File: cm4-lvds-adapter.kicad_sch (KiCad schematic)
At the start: 19 parts, among them J1 Plug_Molex_SlimStack_2x15_538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, J2 JST_SM_1x10_SM10B-SURS-TF-LF-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

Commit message: [#54932] Add changes requested in review
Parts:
- removed C1: C_100n_0402, antmicro-footprints:C_0402_1005Metric, symbol antmicroCapacitors0402:C_100n_0402
- removed TP2, TP4: TP_1mm_SMD, antmicro-footprints:TP_SMD_1mm, symbol antmicroTestPoints:TP_1mm_SMD
- added C1, C6: C_10u_0402, antmicro-footprints:C_0402_1005Metric, symbol antmicroCapacitors0402:C_10u_0402
- added C10, C4, C42, C44, C45, C46, C47, C5, C8, C9: C_100n_0402, antmicro-footprints:C_0402_1005Metric, symbol antmicroCapacitors0402:C_100n_0402
- added C11, C12, C13: C_10n_0402, antmicro-footprints:C_0402_1005Metric, symbol antmicroCapacitors0402:C_10n_0402
- added C14, C7: C_1u_0402, antmicro-footprints:C_0402_1005Metric, symbol antmicroCapacitors0402:C_1u_0402
- added FB1: 220Z/2A, antmicro-footprints:FB_0603_1608Metric, symbol antmicroFerriteBeadsandChips:FB_220Z_2.2A_TDK-MPZ_0603
- added J3: Conn_FFC_Amphenol_62684-402100AHLF, antmicro-footprints:Conn_FFC_Amphenol_1x40_62684-402100AHLF, symbol antmicroFCCConnectors:FFC_Amphenol_1x40_62684-402100AHLF
- added R4, R5, R? (x2): R_4k7_0402, antmicro-footprints:R_0402_1005Metric, symbol antmicroResistors0402:R_4k7_0402
- added R40, R42, R45, R6, R7, R8: R_10k_0402, antmicro-footprints:R_0402_1005Metric, symbol antmicroResistors0402:R_10k_0402
- added R41, R43, R46: R_0R_0402, antmicro-footprints:R_0402_1005Metric, symbol antmicroResistors0402:R_0R_0402
- added R44: R_100k_0402, antmicro-footprints:R_0402_1005Metric, symbol antmicroResistors0402:R_100k_0402
- added TP? (x7): TP_0.75mm_SMD, antmicro-footprints:TP_SMD_0.75mm, symbol antmicroTestPoints:TP_0.75mm_SMD
- added U3: SN65DSI84, antmicro-footprints:HTQFP-64_10x10mm_P0.5mm, symbol antmicroInterfaceControllers:SN65DSI84
- added U?: NTS0104_DHVQFN, antmicro-footprints:DHVQFN-14-1EP_2.5x3mm, symbol antmicroLogicTranslatorsLevelShifters:NTS0104_DHVQFN
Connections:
- net AntmUD.~{RST} is gone; now on net DSICtrl.~{RST}: C43.2, R39.1, TP13.1
- net +3V3: now also C4.2, C47.2, J3.2, J3.3, R40.2, R42.2, R44.2, R45.2, R?.2, U?.14 (VCC_B)
- net +5V: now also C1.2
- net DSI.CLK_N: now also U3.25 (DACN)
- net DSI.CLK_P: now also U3.24 (DACP)
- net DSI.D0_N: now also U3.20 (DA0N)
- net DSI.D0_P: now also U3.19 (DA0P)
- net DSI.D1_N: now also U3.22 (DA1N)
- net DSI.D1_P: now also U3.21 (DA1P)
- net DSI.D2_N: now also U3.28 (DA2N)
- net DSI.D2_P: now also U3.27 (DA2P)
- net DSI.D3_N: now also U3.30 (DA3N)
- net DSI.D3_P: now also U3.29 (DA3P)
- net DSICtrl.EN: now also J3.6, R44.1, U?.11 (B3)
- net DSICtrl.IRQ1: now also R?.1, U?.10 (B4)
- net DSICtrl.SCL: now also U?.12 (B2)
- net DSICtrl.SDA: now also U?.13 (B1)
- net DSICtrl.~{RST}: now also J3.5
- net GND: now also C1.1, C10.1, C11.1, C12.1, C13.1, C14.1, C4.1, C42.1, C44.1, C45.1, C46.1, C47.1, C5.1, C6.1, C7.1, C8.1, C9.1, J3.10, J3.13, J3.16, J3.19, J3.22, J3.25, J3.30, J3.7, J3.SH, R41.2, R43.2, R46.2, R7.1, R8.2, U3.23 (GND), U3.26 (GND), U3.52 (GND), U3.65 (PAD), U?.15 (GNDPAD), U?.7 (GND)
- new net: C10.2, C11.2, C12.2, C13.2, C6.2, C7.2, C8.2, C9.2, FB1.2, U3.14 (VCC), U3.18 (VCC), U3.3 (VCC), U3.32 (VCC), U3.35 (VCC), U3.40 (VCC), U3.43 (VCC), U3.48 (VCC), U3.49 (VCC), U3.55 (VCC), U3.58 (VCC), U3.63 (VCC)
- new net: R6.1, R7.2, U3.64 (ADDR)
- new net: J3.26, TP?.1
- new net: J3.24, TP?.1
- new net: R8.1, U3.17 (REFCLK)
- new net: J3.37, TP?.1
- new net: J3.23, TP?.1
- new net: J3.27, TP?.1
- new net: J3.36, TP?.1
- new net: J3.4, TP?.1
- new net: C14.2, U3.31 (VCORE)
- new net +18V: C42.2, J3.38
- new net +1V8: C5.2, FB1.1, R4.2, R5.2, R6.2, R?.2, U?.1 (VCC_A), U?.8 (OE)
- new net +3V9: C45.2, J3.1
- new net +9V6: C44.2, J3.29
- new net +VLED: C46.2, J3.39, J3.40
- new net -6V: J3.35
- new net -VLED: J3.31, J3.32
- new net DSICtrl_1V8.EN: R?.1, U3.2 (EN), U?.4 (A3)
- new net DSICtrl_1V8.IRQ: U3.33 (IRQ), U?.5 (A4)
- new net DSICtrl_1V8.SCL: R5.1, U3.16 (SDA), U?.3 (A2)
- new net DSICtrl_1V8.SDA: R4.1, U3.15 (SCL), U?.2 (A1)
- new net LVDS.CLK_N: J3.17, U3.39 (A_CLKN)
- new net LVDS.CLK_P: J3.18, U3.38 (A_CLKP)
- new net LVDS.D0_N: J3.8, U3.47 (A_Y0N)
- new net LVDS.D0_P: J3.9, U3.46 (A_Y0P)
- new net LVDS.D1_N: J3.11, U3.45 (A_Y1N)
- new net LVDS.D1_P: J3.12, U3.44 (A_Y1P)
- new net LVDS.D2_N: J3.14, U3.42 (A_Y2N)
- new net LVDS.D2_P: J3.15, U3.41 (A_Y2P)
- new net LVDS.D3_N: J3.20, U3.37 (A_Y3N)
- new net LVDS.D3_P: J3.21, U3.36 (A_Y3P)
- new net SELB: J3.28, R40.1, R41.1
- new net SHLR: J3.33, R42.1, R43.1
- new net UPDN: J3.34, R45.1, R46.1
- no-connect marks 8 -> 18
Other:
- sheet LVDS display renamed Power
- removed sheet DSI -> LVDS converter
- sheet Power: file lvds.kicad_sch -> power.kicad_sch
- sheet Power ports: added none; removed LVDS{LVDS}
- note added: "Display configuration"
- note added: "Display decoupling capacitors"
- note added: "Max 45mA"
- note added: "Note: I_{2}C address selection: ADDR | write address 1 | 0x5A 0 | 0x58"
- note added: "Note: SN65DSI83*-Q1 should be here drop-in compatible"
- note added: "Set display orientation as NORMAL datasheet pg.10"
- note added: "VDD"
- note added: "Vcom"
- note added: "https://drive.google.com/file/d/1bkluVrM0Or-iIsGhq6TyBP5G7xjQ2-Zj/view"
- note added: "select 8bit input"
- moved on the sheet: C43, D1, D2, D3, D4, J1, J2, R1, R2, R39

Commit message: [#54932] Clean ERC
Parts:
- gave numbers to parts that had none: 10
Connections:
- net DSICtrl_1V8.IRQ: no longer U2.5 (A4)
- new net DSICtrl_1V8.IRQ1: U2.5 (A4)
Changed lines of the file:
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@@
     (effects (font (size 1.27 1.27)) (justify right bottom))
   )
-  (label "DSICtrl_1V8.IRQ" (at 161.29 190.5 0) (fields_autoplaced)
+  (label "DSICtrl_1V8.IRQ1" (at 161.29 190.5 0) (fields_autoplaced)
     (effects (font (size 1.27 1.27)) (justify left bottom))
   )
@@
   (symbol (lib_id "antmicroTestPoints:TP_0.75mm_SMD") (at 388.62 161.29 180) (unit 1)
     (in_bom yes) (on_board yes) (dnp no)
-    (property "Reference" "TP?" (at 382.27 161.29 0)
+    (property "Reference" "TP9" (at 382.27 161.29 0)
       (effects (font (size 1.27 1.27) (thickness 0.15)))
     )
@@
       (project "cm4-lvds-adapter"
         (path "/60b842dc-0853-4a25-99ac-5784ddf94d0d"
-          (reference "TP?") (unit 1)
+          (reference "TP9") (unit 1)
         )
       )
@@
   (symbol (lib_id "antmicroTestPoints:TP_0.75mm_SMD") (at 388.62 156.21 180) (unit 1)
     (in_bom yes) (on_board yes) (dnp no)
-    (property "Reference" "TP?" (at 382.27 156.21 0)
+    (property "Reference" "TP8" (at 382.27 156.21 0)
       (effects (font (size 1.27 1.27) (thickness 0.15)))
     )
@@
       (project "cm4-lvds-adapter"
         (path "/60b842dc-0853-4a25-99ac-5784ddf94d0d"
-          (reference "TP?") (unit 1)
+          (reference "TP8") (unit 1)
         )
       )
@@
   (symbol (lib_id "antmicroLogicTranslatorsLevelShifters:NTS0104_DHVQFN") (at 140.97 177.8 0) (mirror y) (unit 1)
     (in_bom yes) (on_board yes) (dnp no)
-    (property "Reference" "U?" (at 130.81 170.18 0)
+    (property "Reference" "U2" (at 130.81 170.18 0)
       (effects (font (size 1.27 1.27) (thickness 0.15)))
     )
@@
       (project "cm4-lvds-adapter"
         (path "/60b842dc-0853-4a25-99ac-5784ddf94d0d"
-          (reference "U?") (unit 1)
+          (reference "U2") (unit 1)
         )
       )
@@
   (symbol (lib_id "antmicroTestPoints:TP_0.75mm_SMD") (at 388.62 189.23 180) (unit 1)
     (in_bom yes) (on_board yes) (dnp no)
-    (property "Reference" "TP?" (at 382.27 189.23 0)
+    (property "Reference" "TP15" (at 382.27 189.23 0)
       (effects (font (size 1.27 1.27) (thickness 0.15)))
     )
@@
       (project "cm4-lvds-adapter"
         (path "/60b842dc-0853-4a25-99ac-5784ddf94d0d"
-          (reference "TP?") (unit 1)
+          (reference "TP15") (unit 1)
         )
       )
@@
   (symbol (lib_id "antmicroTestPoints:TP_0.75mm_SMD") (at 388.62 153.67 180) (unit 1)
     (in_bom yes) (on_board yes) (dnp no)
-    (property "Reference" "TP?" (at 382.27 153.67 0)
+    (property "Reference" "TP4" (at 382.27 153.67 0)
       (effects (font (size 1.27 1.27) (thickness 0.15)))
     )
@@
       (project "cm4-lvds-adapter"
         (path "/60b842dc-0853-4a25-99ac-5784ddf94d0d"
-          (reference "TP?") (unit 1)
+          (reference "TP4") (unit 1)
         )
       )
@@
   (symbol (lib_id "antmicroTestPoints:TP_0.75mm_SMD") (at 388.62 163.83 180) (unit 1)
     (in_bom yes) (on_board yes) (dnp no)
-    (property "Reference" "TP?" (at 382.27 163.83 0)
+    (property "Reference" "TP12" (at 382.27 163.83 0)
       (effects (font (size 1.27 1.27) (thickness 0.15)))
     )
@@
       (project "cm4-lvds-adapter"
         (path "/60b842dc-0853-4a25-99ac-5784ddf94d0d"
-          (reference "TP?") (unit 1)
+          (reference "TP12") (unit 1)
         )
       )
@@
   (symbol (lib_id "antmicroTestPoints:TP_0.75mm_SMD") (at 388.62 186.69 180) (unit 1)
     (in_bom yes) (on_board yes) (dnp no)
-    (property "Reference" "TP?" (at 382.27 186.69 0)
+    (property "Reference" "TP14" (at 382.27 186.69 0)
       (effects (font (size 1.27 1.27) (thickness 0.15)))
     )
@@
       (project "cm4-lvds-adapter"
         (path "/60b842dc-0853-4a25-99ac-5784ddf94d0d"
-          (reference "TP?") (unit 1)
+          (reference "TP14") (unit 1)
         )
       )
@@
   (symbol (lib_id "antmicroResistors0402:R_4k7_0402") (at 156.21 181.61 90) (unit 1)
     (in_bom yes) (on_board yes) (dnp no)
-    (property "Reference" "R?" (at 157.48 177.8 90)
+    (property "Reference" "R48" (at 157.48 177.8 90)
       (effects (font (size 1.27 1.27) (thickness 0.15)) (justify right))
     )
@@
       (project "cm4-lvds-adapter"
         (path "/60b842dc-0853-4a25-99ac-5784ddf94d0d"
-          (reference "R?") (unit 1)
+          (reference "R48") (unit 1)
         )
       )
@@
   (symbol (lib_id "antmicroResistors0402:R_4k7_0402") (at 114.3 181.61 90) (unit 1)
     (in_bom yes) (on_board yes) (dnp no)
-    (property "Reference" "R?" (at 115.57 177.8 90)
+    (property "Reference" "R47" (at 115.57 177.8 90)
       (effects (font (size 1.27 1.27) (thickness 0.15)) (justify right))
     )
@@
       (project "cm4-lvds-adapter"
         (path "/60b842dc-0853-4a25-99ac-5784ddf94d0d"
-          (reference "R?") (unit 1)
+          (reference "R47") (unit 1)
         )
       )
@@
   (symbol (lib_id "antmicroTestPoints:TP_0.75mm_SMD") (at 388.62 105.41 180) (unit 1)
     (in_bom yes) (on_board yes) (dnp no)
-    (property "Reference" "TP?" (at 384.81 102.87 0)
+    (property "Reference" "TP2" (at 384.81 102.87 0)
       (effects (font (size 1.27 1.27) (thickness 0.15)) (justify bottom))
     )
@@
       (project "cm4-lvds-adapter"
         (path "/60b842dc-0853-4a25-99ac-5784ddf94d0d"
-          (reference "TP?") (unit 1)
+          (reference "TP2") (unit 1)
         )
       )

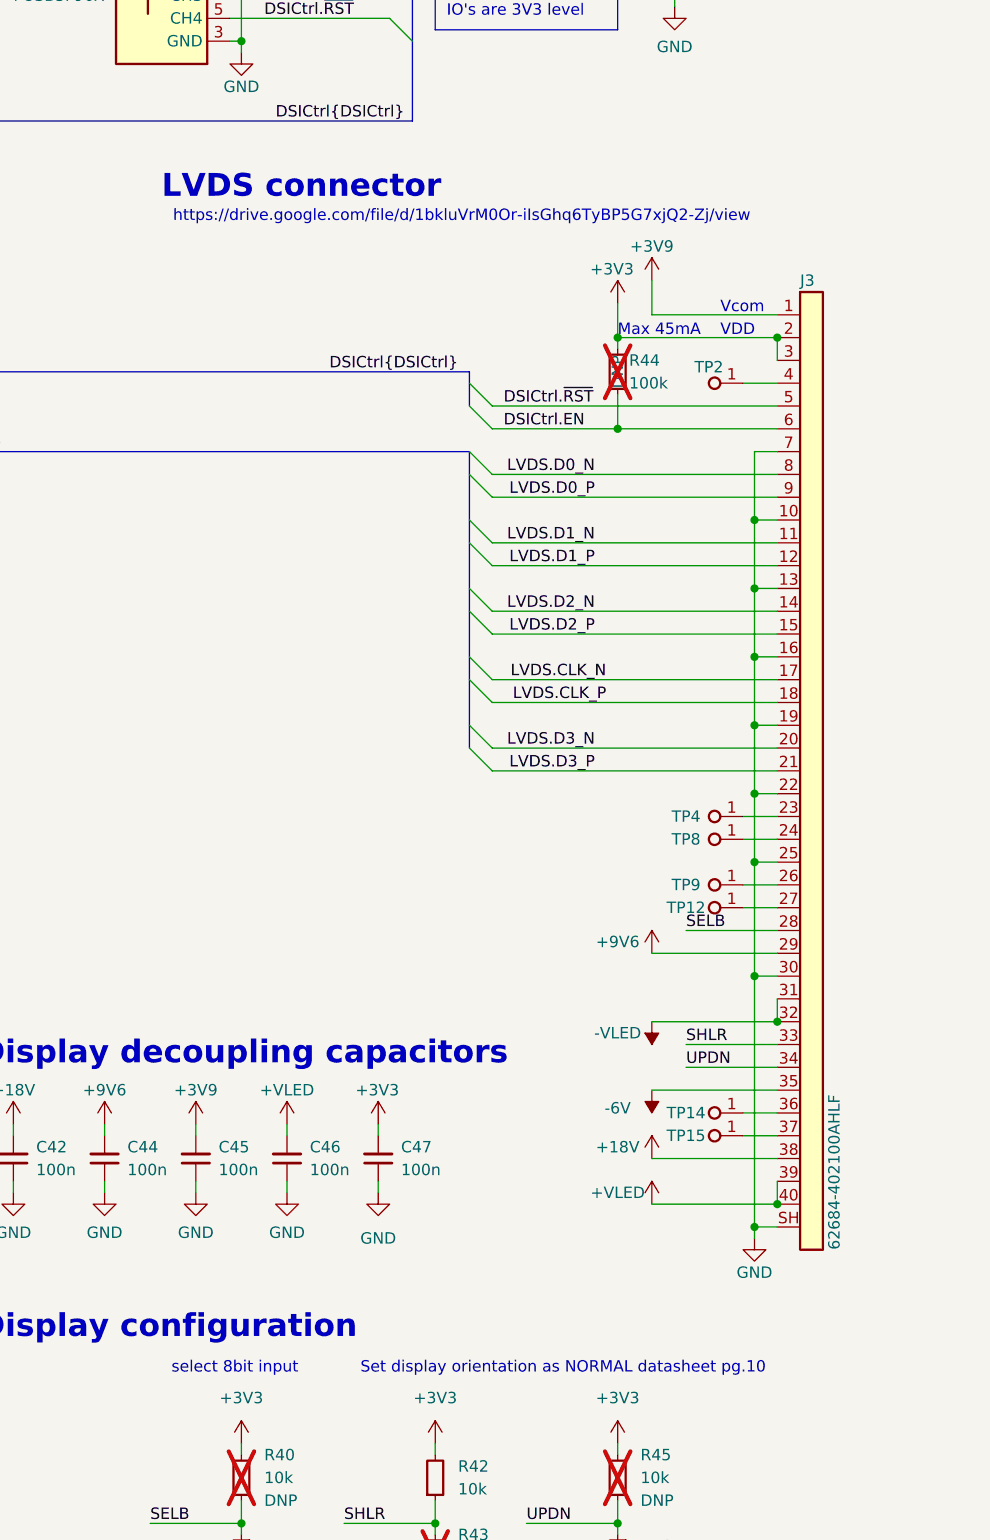
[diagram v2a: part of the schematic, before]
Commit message: [#54932] Change information regarding used display
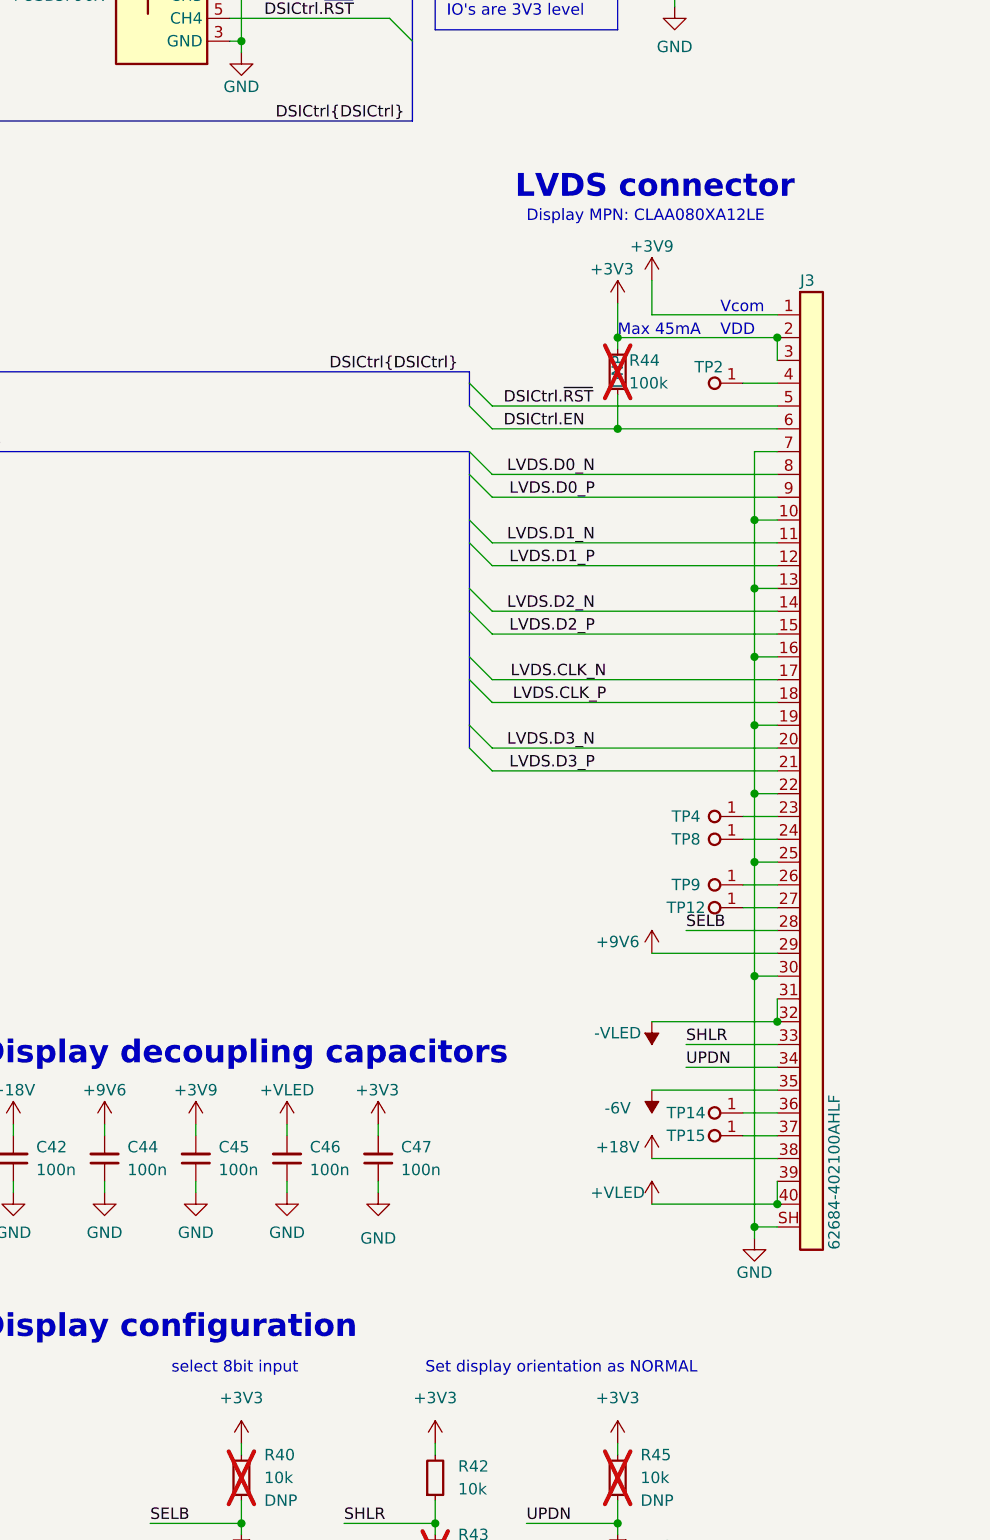
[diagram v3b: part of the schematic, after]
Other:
- note added: "Display MPN: CLAA080XA12LE"
- note added: "Set display orientation as NORMAL"
- note removed: "Set display orientation as NORMAL datasheet pg.10"
- note removed: "https://drive.google.com/file/d/1bkluVrM0Or-iIsGhq6TyBP5G7xjQ2-Zj/view"
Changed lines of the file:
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@@
     (effects (font (size 2.54 2.54) (thickness 0.508) bold) (justify left bottom))
   )
-  (text "LVDS connector" (at 323.85 85.09 0)
+  (text "LVDS connector" (at 363.22 85.09 0)
     (effects (font (size 2.54 2.54) (thickness 0.508) bold) (justify left bottom))
   )
@@
     (effects (font (size 1.27 1.27)) (justify left bottom))
   )
-  (text "Set display orientation as NORMAL datasheet pg.10" (at 391.16 215.9 0)
+  (text "Set display orientation as NORMAL" (at 383.54 215.9 0)
     (effects (font (size 1.27 1.27)) (justify right bottom))
   )
@@
     (effects (font (size 2.54 2.54) (thickness 0.508) bold) (justify left bottom))
   )
-  (text "https://drive.google.com/file/d/1bkluVrM0Or-iIsGhq6TyBP5G7xjQ2-Zj/view"
-    (at 325.12 87.63 0)
+  (text "Display MPN: CLAA080XA12LE" (at 364.49 87.63 0)
     (effects (font (size 1.27 1.27)) (justify left bottom))
   )
